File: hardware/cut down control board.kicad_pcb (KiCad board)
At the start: 2 copper layers, 17 parts, among them J1 Conn_01x02, J2 Conn_01x02, J3 AVR-ISP-6, J5 Conn_01x06_Female, J7 Conn_01x06_Male, Q1 FQP30N06L, Q2 FQP30N06L, U1 ATmega328-P, U2 MPL3115A2, U5 L78L33_TO92

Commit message: testing github change
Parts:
- moved J1 8.03 mm to (109.2, 132.1)
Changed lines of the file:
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@@
     (fp_line (start -2.566921 -8.53) (end 41.54 -8.53) (layer "F.SilkS") (width 0.12))
     (fp_line (start -1.846921 7.655066) (end 16.153079 7.655066) (layer "F.SilkS") (width 0.12))
-    (fp_arc (start 33.953079 5.655066) (mid 35.367318 6.240843) (end 35.953079 7.655066) (layer "F.SilkS") (width 0.12))
-    (fp_arc (start 16.153079 7.655066) (mid 16.738863 6.240848) (end 18.153079 5.655066) (layer "F.SilkS") (width 0.12))
-    (fp_arc (start 35.953079 -7.544934) (mid 35.367294 -6.130718) (end 33.953079 -5.544934) (layer "F.SilkS") (width 0.12))
-    (fp_arc (start 18.153079 -5.544934) (mid 16.738891 -6.13073) (end 16.153079 -7.544934) (layer "F.SilkS") (width 0.12))
+    (fp_arc (start 33.953079 5.655066) (mid 35.367283 6.240849) (end 35.953079 7.655066) (layer "F.SilkS") (width 0.12))
+    (fp_arc (start 16.153079 7.655066) (mid 16.73886 6.240845) (end 18.153079 5.655066) (layer "F.SilkS") (width 0.12))
+    (fp_arc (start 35.953079 -7.544934) (mid 35.367293 -6.130722) (end 33.953079 -5.544934) (layer "F.SilkS") (width 0.12))
+    (fp_arc (start 18.153079 -5.544934) (mid 16.738885 -6.130739) (end 16.153079 -7.544934) (layer "F.SilkS") (width 0.12))
     (fp_line (start 41.64 8.65) (end -2.696921 8.65) (layer "F.CrtYd") (width 0.05))
     (fp_line (start -2.696921 -8.65) (end 41.64 -8.65) (layer "F.CrtYd") (width 0.05))
@@
   )
   (footprint "Connector_JST:JST_XH_B2B-XH-A_1x02_P2.50mm_Vertical" (layer "F.Cu")
-    (at 101.6 134.62)
+    (at 109.22 132.08)
     (descr "JST XH series connector, B2B-XH-A (http://www.jst-mfg.com/product/pdf/eng/eXH.pdf), generated with kicad-footprint-generator")
     (tags "connector JST XH vertical")
@@
     (fp_line (start 41.54 -8.53) (end 41.54 8.53) (layer "F.SilkS") (width 0.12))
     (fp_line (start 35.953079 -7.65) (end 40.64 -7.65) (layer "F.SilkS") (width 0.12))
-    (fp_arc (start 35.953079 -7.544934) (mid 35.367294 -6.130718) (end 33.953079 -5.544934) (layer "F.SilkS") (width 0.12))
-    (fp_arc (start 33.953079 5.655066) (mid 35.367318 6.240843) (end 35.953079 7.655066) (layer "F.SilkS") (width 0.12))
-    (fp_arc (start 16.153079 7.655066) (mid 16.738863 6.240848) (end 18.153079 5.655066) (layer "F.SilkS") (width 0.12))
-    (fp_arc (start 18.153079 -5.544934) (mid 16.738891 -6.13073) (end 16.153079 -7.544934) (layer "F.SilkS") (width 0.12))
+    (fp_arc (start 35.953079 -7.544934) (mid 35.367293 -6.130722) (end 33.953079 -5.544934) (layer "F.SilkS") (width 0.12))
+    (fp_arc (start 33.953079 5.655066) (mid 35.367283 6.240849) (end 35.953079 7.655066) (layer "F.SilkS") (width 0.12))
+    (fp_arc (start 16.153079 7.655066) (mid 16.73886 6.240845) (end 18.153079 5.655066) (layer "F.SilkS") (width 0.12))
+    (fp_arc (start 18.153079 -5.544934) (mid 16.738885 -6.130739) (end 16.153079 -7.544934) (layer "F.SilkS") (width 0.12))
     (fp_line (start -2.696921 -8.65) (end 41.64 -8.65) (layer "F.CrtYd") (width 0.05))
     (fp_line (start 41.64 8.65) (end -2.696921 8.65) (layer "F.CrtYd") (width 0.05))
@@
     (fp_line (start 33.953079 5.655066) (end 18.153079 5.655066) (layer "F.SilkS") (width 0.12))
     (fp_line (start -2.566921 8.53) (end -2.566921 -8.53) (layer "F.SilkS") (width 0.12))
-    (fp_arc (start 33.953079 5.655066) (mid 35.367318 6.240843) (end 35.953079 7.655066) (layer "F.SilkS") (width 0.12))
-    (fp_arc (start 18.153079 -5.544934) (mid 16.738891 -6.13073) (end 16.153079 -7.544934) (layer "F.SilkS") (width 0.12))
-    (fp_arc (start 16.153079 7.655066) (mid 16.738863 6.240848) (end 18.153079 5.655066) (layer "F.SilkS") (width 0.12))
-    (fp_arc (start 35.953079 -7.544934) (mid 35.367294 -6.130718) (end 33.953079 -5.544934) (layer "F.SilkS") (width 0.12))
+    (fp_arc (start 33.953079 5.655066) (mid 35.367283 6.240849) (end 35.953079 7.655066) (layer "F.SilkS") (width 0.12))
+    (fp_arc (start 18.153079 -5.544934) (mid 16.738885 -6.130739) (end 16.153079 -7.544934) (layer "F.SilkS") (width 0.12))
+    (fp_arc (start 16.153079 7.655066) (mid 16.73886 6.240845) (end 18.153079 5.655066) (layer "F.SilkS") (width 0.12))
+    (fp_arc (start 35.953079 -7.544934) (mid 35.367293 -6.130722) (end 33.953079 -5.544934) (layer "F.SilkS") (width 0.12))
     (fp_line (start -2.696921 8.65) (end -2.696921 -8.65) (layer "F.CrtYd") (width 0.05))
     (fp_line (start 41.64 -8.65) (end 41.64 8.65) (layer "F.CrtYd") (width 0.05))

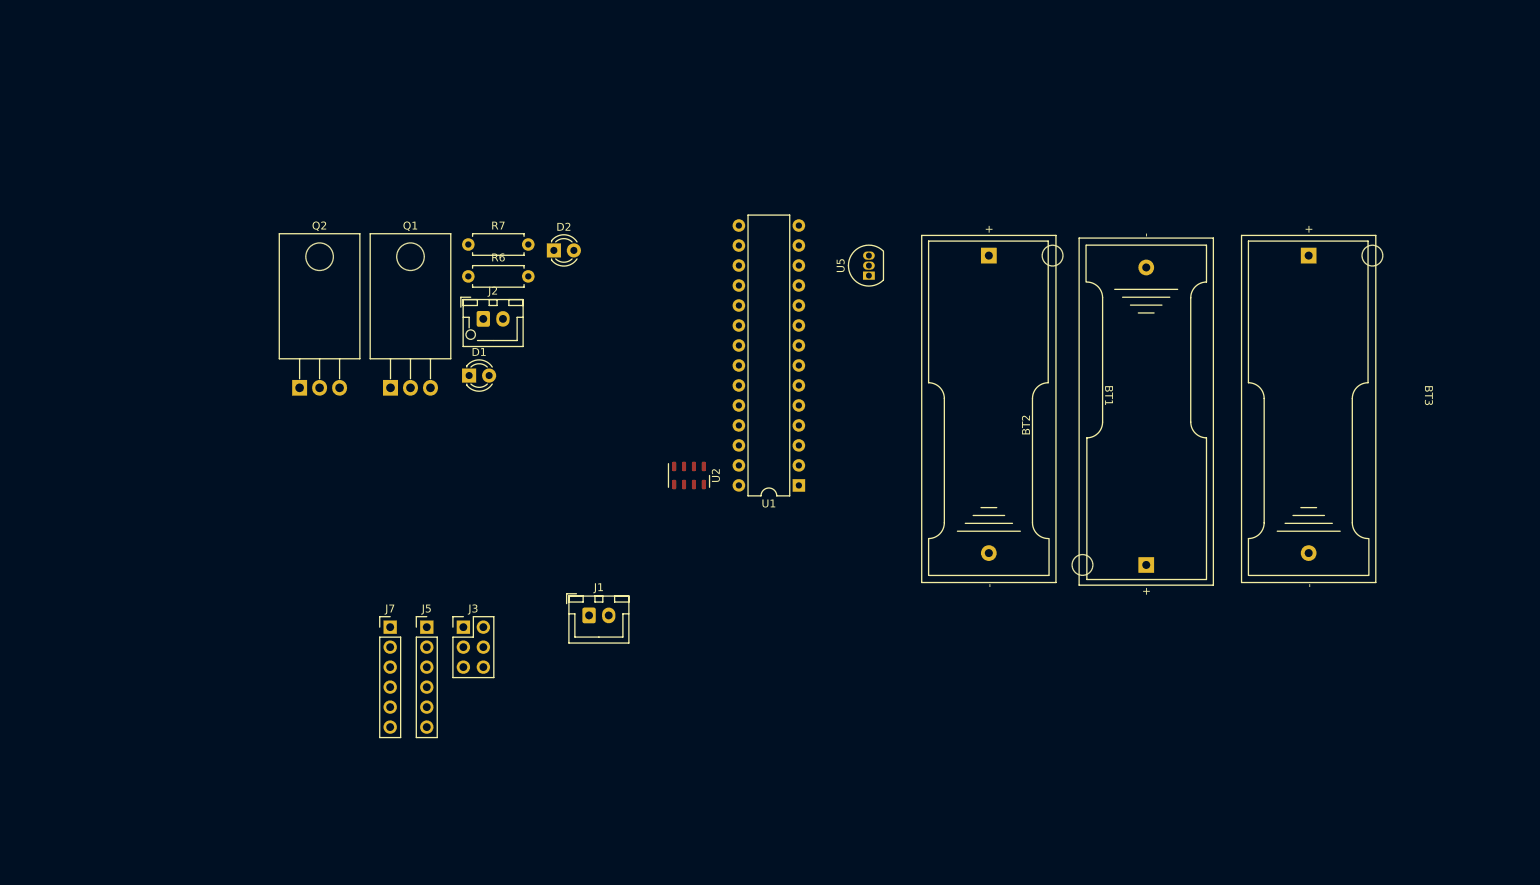
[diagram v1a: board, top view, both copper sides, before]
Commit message: added footprints
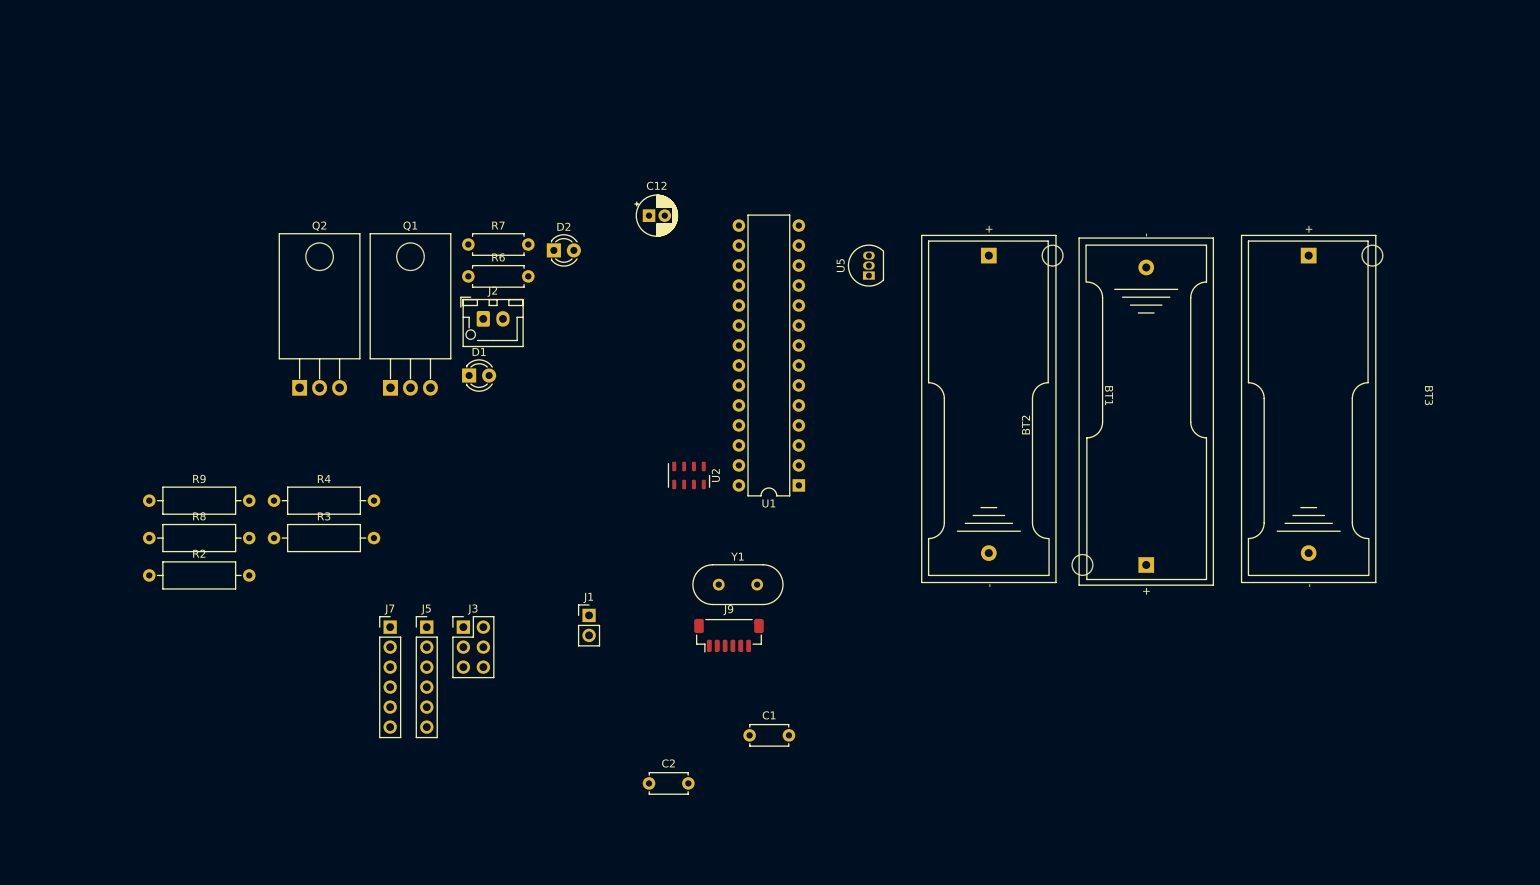
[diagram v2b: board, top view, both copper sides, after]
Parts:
- added C1: 22pF, Capacitor_THT:C_Disc_D4.7mm_W2.5mm_P5.00mm, F.Cu at (129.6, 147.3)
- added C12: 10uF, Capacitor_THT:CP_Radial_D5.0mm_P2.00mm, F.Cu at (116.8, 81.3)
- added C2: 22pF, Capacitor_THT:C_Disc_D4.7mm_W2.5mm_P5.00mm, F.Cu at (116.8, 153.4)
- added J9: Conn_01x06, Connector_JST:JST_SH_BM06B-SRSS-TB_1x06-1MP_P1.00mm_Vertical, F.Cu at (127.0, 134.6)
- added R2: 10K, Resistor_THT:R_Axial_DIN0309_L9.0mm_D3.2mm_P12.70mm_Horizontal, F.Cu at (53.3, 127.0)
- added R3: 10K, Resistor_THT:R_Axial_DIN0309_L9.0mm_D3.2mm_P12.70mm_Horizontal, F.Cu at (69.2, 122.2)
- added R4: 100K, Resistor_THT:R_Axial_DIN0309_L9.0mm_D3.2mm_P12.70mm_Horizontal, F.Cu at (69.2, 117.5)
- added R8: 1K, Resistor_THT:R_Axial_DIN0309_L9.0mm_D3.2mm_P12.70mm_Horizontal, F.Cu at (53.3, 122.2)
- added R9: 1K, Resistor_THT:R_Axial_DIN0309_L9.0mm_D3.2mm_P12.70mm_Horizontal, F.Cu at (53.3, 117.5)
- added Y1: 16MHz, Crystal:Crystal_HC49-4H_Vertical, F.Cu at (125.7, 128.2)
- J1: footprint Connector_JST:JST_XH_B2B-XH-A_1x02_P2.50mm_Vertical -> Connector_PinHeader_2.54mm:PinHeader_1x02_P2.54mm_Vertical
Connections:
- J5 pad 1: /TX_SAT -> GND
- J5 pad 2: /RX_SAT -> /SLEEP
- J5 pad 4: /SLEEP -> /TX_SAT
- J5 pad 5: /RING -> /RX_SAT
- J5 pad 6: GND -> /RING
- J7 pad 4: /TX_DBG -> /RX_DBG
- J7 pad 5: /RX_DBG -> /TX_DBG

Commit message: update pcb layout
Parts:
- added C10: 100nF, Capacitor_THT:C_Axial_L5.1mm_D3.1mm_P7.50mm_Horizontal, F.Cu at (153.7, 137.2)
- added C11: 1uF, Capacitor_THT:C_Axial_L5.1mm_D3.1mm_P7.50mm_Horizontal, F.Cu at (38.1, 88.9)
- added C3: 100nF, Capacitor_THT:C_Axial_L5.1mm_D3.1mm_P7.50mm_Horizontal, F.Cu at (120.7, 121.9)
- added C4: 100nF, Capacitor_THT:C_Axial_L5.1mm_D3.1mm_P7.50mm_Horizontal, F.Cu at (138.5, 124.5)
- added C5: 100nF, Capacitor_THT:C_Axial_L5.1mm_D3.1mm_P7.50mm_Horizontal, F.Cu at (72.5, 81.3)
- added C6: 0.33uF, Capacitor_THT:C_Axial_L5.1mm_D3.1mm_P7.50mm_Horizontal, F.Cu at (138.5, 162.6)
- added C7: 0.33uF, Capacitor_THT:C_Axial_L5.1mm_D3.1mm_P7.50mm_Horizontal, F.Cu at (163.9, 147.3)
- added C8: 0.1uF, Capacitor_THT:C_Axial_L5.1mm_D3.1mm_P7.50mm_Horizontal, F.Cu at (138.5, 137.2)
- added C9: 0.1uF, Capacitor_THT:C_Axial_L5.1mm_D3.1mm_P7.50mm_Horizontal, F.Cu at (163.9, 162.6)
- added J10: SAT(10 picoblade), Connector_Molex:Molex_PicoBlade_53047-1010_1x10_P1.25mm_Vertical, F.Cu at (73.7, 147.3)
- added J11: VGPS SELECT, Jumper:SolderJumper-3_P1.3mm_Bridged12_RoundedPad1.0x1.5mm, F.Cu at (114.3, 142.2)
- added J6: GPS(PIN HDR), Connector_PinSocket_2.54mm:PinSocket_1x04_P2.54mm_Vertical, F.Cu at (121.9, 142.2)
- added R1: 10K, Resistor_THT:R_Axial_DIN0309_L9.0mm_D3.2mm_P12.70mm_Horizontal, F.Cu at (59.7, 91.4)
- added R5: 33K, Resistor_THT:R_Axial_DIN0309_L9.0mm_D3.2mm_P12.70mm_Horizontal, F.Cu at (95.2, 99.1)
- added U6: L7805, Package_TO_SOT_THT:TO-220-3_Horizontal_TabDown, F.Cu at (114.3, 103.2)
- J1: value Conn_01x02 -> CUTTER
- J2: value Conn_01x02 -> MOTOR
- J5: value Conn_01x06_Female -> SAT(PIN HDR)
- J7: value Conn_01x06_Male -> DBG TTL
- J9: value Conn_01x06 -> GPS(JST SH)
- moved C1 77.3 mm to (61.0, 111.8), turned to 180 degrees
- moved C12 71.8 mm to (45.7, 91.4), turned to -90 degrees
- moved C2 66.2 mm to (61.0, 117.9), turned to 180 degrees
- moved U1 62.7 mm to (77.5, 92.7), turned to 0 degrees
- moved R8 60.4 mm to (95.2, 78.7)
- moved Y1 60.3 mm to (66.2, 117.9), turned to 90 degrees
- moved Q1 55.7 mm to (139.7, 103.2)
- moved Q2 54.6 mm to (127.0, 103.2)
- moved R9 51.3 mm to (80.0, 73.7)
- moved J2 49.6 mm to (142.2, 111.8), turned to 90 degrees
- moved R4 47.8 mm to (109.2, 91.4), turned to 180 degrees
- moved R3 41.6 mm to (85.1, 83.8)
- moved U2 36.6 mm to (91.4, 94.0), turned to 0 degrees
- moved R6 32.9 mm to (94.0, 121.9), turned to -90 degrees
- moved U5 32.1 mm to (134.6, 119.4)
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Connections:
- C2 pad 1: Net-(C2-Pad1) -> Net-(U1-Pad10)
- J9 pad 2: +5V -> /+VGPS
- Q1 pad 3: Net-(Q1-Pad3) -> GND
- R2 pad 2: Net-(Q1-Pad3) -> GND
- U1 pad 10: Net-(C2-Pad1) -> Net-(U1-Pad10)
- Y1 pad 1: unconnected-(Y1-Pad1) -> Net-(U1-Pad10)
- Y1 pad 2: unconnected-(Y1-Pad2) -> Net-(C1-Pad1)

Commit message: More updates to PCB
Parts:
- J1: footprint Connector_PinHeader_2.54mm:PinHeader_1x02_P2.54mm_Vertical -> Connector_JST:JST_XH_B2B-XH-A_1x02_P2.50mm_Vertical
- J2: footprint Connector_JST:JST_XH_B2B-XH-AM_1x02_P2.50mm_Vertical -> Connector_JST:JST_XH_B2B-XH-A_1x02_P2.50mm_Vertical
- moved J6 28.1 mm to (94.0, 144.8)
- moved J9 25.5 mm to (99.1, 137.2)
- moved U5 16.1 mm to (119.4, 114.3)
- turned J1 to 90 degrees

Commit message: board layout
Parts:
- D1: value LED, RED -> RED
- D2: value LED, GREEN -> GRN
- J2: footprint Connector_JST:JST_XH_B2B-XH-A_1x02_P2.50mm_Vertical -> Connector_JST:JST_XH_B2B-XH-AM_1x02_P2.50mm_Vertical
- R1, R2, R3, R4, R5, R8, R9: footprint Resistor_THT:R_Axial_DIN0309_L9.0mm_D3.2mm_P12.70mm_Horizontal -> Resistor_THT:R_Axial_DIN0204_L3.6mm_D1.6mm_P7.62mm_Horizontal
- R6, R7: footprint Resistor_THT:R_Axial_DIN0207_L6.3mm_D2.5mm_P7.62mm_Horizontal -> Resistor_THT:R_Axial_DIN0204_L3.6mm_D1.6mm_P7.62mm_Horizontal
- U5: value L78L33_TO92 -> L78L33
- moved R2 138.9 mm to (164.7, 82.9), turned to -90 degrees
- moved C11 101.7 mm to (137.3, 66.3), turned to 90 degrees
- moved C12 101.7 mm to (143.8, 64.4), turned to 90 degrees
- moved J10 89.0 mm to (104.1, 63.7), turned to -90 degrees
- moved C5 73.8 mm to (145.2, 69.3), turned to -90 degrees
- moved BT2 70.3 mm to (205.4, 60.1), turned to -90 degrees
- moved C6 69.4 mm to (157.8, 95.9), turned to 180 degrees
- moved C10 69.4 mm to (140.1, 69.1), turned to -90 degrees
- moved R1 68.6 mm to (122.2, 63.2), turned to 180 degrees
- moved J5 67.1 mm to (110.2, 75.4), turned to 180 degrees
- moved R3 64.8 mm to (149.9, 82.5), turned to -90 degrees
- moved D1 58.1 mm to (133.0, 80.6), turned to -90 degrees
- moved C2 56.8 mm to (110.9, 90.8), turned to -90 degrees
- moved C9 55.5 mm to (153.5, 108.1), turned to 90 degrees
- moved C1 55.2 mm to (110.9, 88.3), turned to 90 degrees
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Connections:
- R1 pad 1: unconnected-(R1-Pad1) -> +3.3V
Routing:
- net +9V: track 0.00 -> 65.8 mm
- net +3.3V: track 0.00 -> 50.5 mm
- net /RING: track 0.00 -> 33.1 mm
- net +5V: track 0.00 -> 31.0 mm
- net /SCK: track 0.00 -> 23.2 mm
- net Net-(BT1-Pad2): track 0.00 -> 20.0 mm
- net /+VGPS: track 0.00 -> 18.1 mm
- net /TX_DBG: track 0.00 -> 17.0 mm
- net /RX_DBG: track 0.00 -> 17.0 mm
- net Net-(BT2-Pad2): track 0.00 -> 16.2 mm
- net /SCL: track 0.00 -> 15.2 mm
- net /MOSI: track 0.00 -> 14.8 mm
- net /TX_SAT: track 0.00 -> 14.0 mm
- net /SLEEP: track 0.00 -> 13.8 mm
- net /RX_SAT: track 0.00 -> 13.8 mm
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- added copper zone on B.Cu, net GND

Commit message: changed footprint J2
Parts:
- J2: footprint Connector_JST:JST_XH_B2B-XH-AM_1x02_P2.50mm_Vertical -> Connector_JST:JST_XH_B2B-XH-A_1x02_P2.50mm_Vertical
- U5: value L78L33 -> L78L33_TO92
- moved C8 1.67 mm to (144.5, 108.7)
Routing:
- net +3.3V: track 50.5 -> 53.6 mm
- net +5V: track 31.0 -> 32.9 mm

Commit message: finished board, generated gerbers
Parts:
- removed C3: 100nF, Capacitor_THT:C_Axial_L5.1mm_D3.1mm_P7.50mm_Horizontal
- added ?: , , F.Cu at (151.8, 126.3)
- added ?: , , F.Cu at (80.7, 72.3)
- added ?: , , F.Cu at (80.7, 126.3)
- added ?: , , F.Cu at (151.8, 72.3)
- added ?: , , F.Cu at (223.0, 126.3)
- added ?: , , F.Cu at (223.0, 72.3)
- added J12: Analog In, Connector_PinHeader_2.54mm:PinHeader_2x03_P2.54mm_Vertical, F.Cu at (105.7, 90.6)
- added SW1: SW_SPST, Connector_JST:JST_XH_B2B-XH-A_1x02_P2.50mm_Vertical, F.Cu at (135.1, 107.1)
- J3: value AVR-ISP-6 -> ISP
- J6: footprint Connector_PinSocket_2.54mm:PinSocket_1x04_P2.54mm_Vertical -> Connector_PinHeader_2.54mm:PinHeader_1x04_P2.54mm_Vertical
- moved C7 48.1 mm to (127.1, 105.7), turned to 90 degrees
- moved J9 44.6 mm to (79.5, 114.5), turned to 90 degrees
- moved C5 37.1 mm to (114.2, 89.5), turned to 0 degrees
- moved D2 37.0 mm to (110.0, 113.6), turned to 180 degrees
- moved J6 34.4 mm to (85.7, 118.4), turned to 180 degrees
- moved R6 33.5 mm to (108.7, 109.4), turned to 90 degrees
- moved C9 33.2 mm to (127.1, 87.9), turned to -90 degrees
- moved D1 32.5 mm to (105.7, 98.3), turned to 0 degrees
- moved C4 31.5 mm to (100.6, 104.2), turned to 90 degrees
- moved U6 30.8 mm to (133.7, 98.1), turned to 0 degrees
- moved R9 30.7 mm to (104.8, 85.3)
- moved C10 30.2 mm to (114.7, 85.4), turned to 90 degrees
- moved U2 29.9 mm to (108.7, 85.1)
- moved R1 29.9 mm to (96.9, 79.2)
- moved J5 29.9 mm to (84.9, 91.4)
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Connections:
- BT1 pad 1: +9V -> VDD
- J1 pad 1: +9V -> VDD
- J11 pad 1: +5V -> +3.3V
- J11 pad 3: +3.3V -> +5V
- J2 pad 1: +9V -> VDD
- U1 pad 12: /RX_DBG -> /RX_GPS
- U1 pad 13: /TX_DBG -> /TX_GPS
- U1 pad 15: /TX_GPS -> /TX_DBG
- U1 pad 16: /RX_GPS -> /RX_DBG
- U1 pad 23: unconnected-(U1-Pad23) -> /A0
- U1 pad 24: unconnected-(U1-Pad24) -> /A1
- U1 pad 25: unconnected-(U1-Pad25) -> /A2
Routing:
- net /CUTTER: track 4.79 -> 76.0 mm
- net +3.3V: track 53.6 -> 122.2 mm
- net /LETDOWN_MOTOR: track 4.29 -> 63.1 mm
- net VDD: track 0.00 -> 50.8 mm
- net /RESET: track 4.70 -> 55.3 mm, vias 0 -> 1
- net +5V: track 32.9 -> 77.9 mm
- net /+VGPS: track 18.1 -> 52.9 mm
- net +9V: track 65.9 -> 37.6 mm
- net GND: track 7.91 -> 31.1 mm, vias 1 -> 0
- net /BATT_SENSE: track 6.81 -> 21.3 mm
- net /A0: track 0.00 -> 12.6 mm
- net /TX_DBG: track 17.0 -> 7.01 mm
- net /A1: track 0.00 -> 7.72 mm
- net /RX_DBG: track 17.0 -> 10.6 mm
- net Net-(D1-Pad2): track 10.0 -> 3.65 mm
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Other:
- board outline added: 152.4 x 63.7 mm
- board text added: "https://github.com/dwkennedy/ballooning 10/11/2022"
